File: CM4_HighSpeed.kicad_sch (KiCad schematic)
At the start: 13 parts, among them J10 690-019-298-412, J15 Conn_01x22_Female, J16 Conn_01x22_Female, J22 690-019-298-412, J4 Conn_01x22_Female, J5 Conn_01x22_Female, J6 THD-02-R, U12 RT9742SNGV

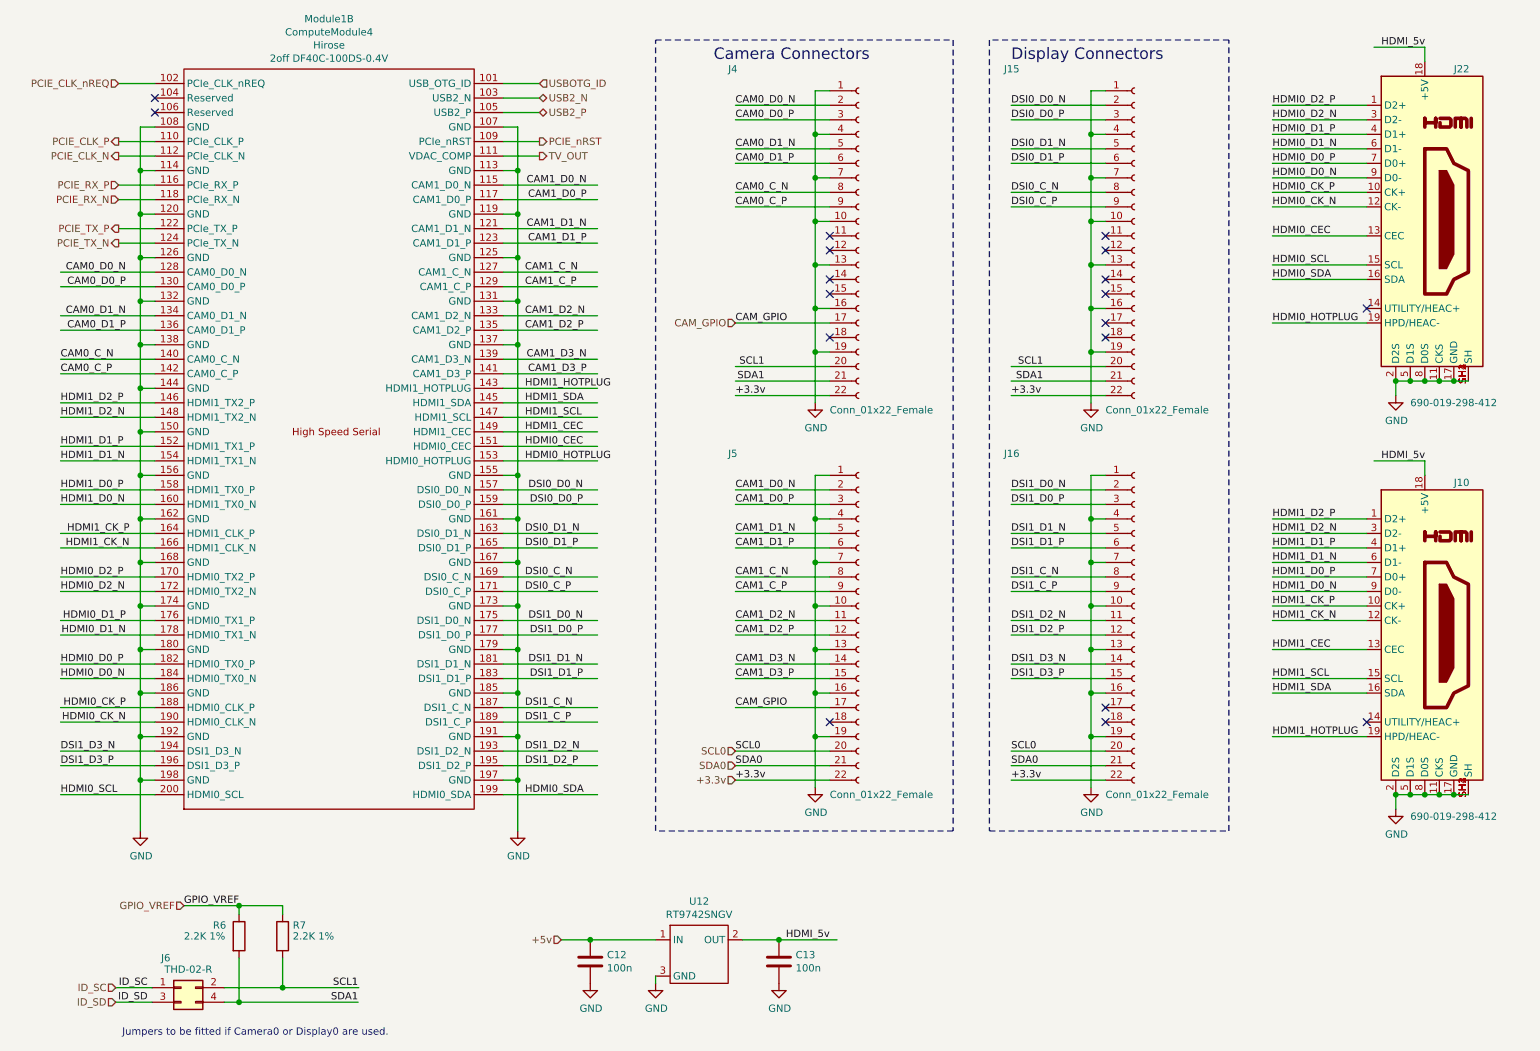
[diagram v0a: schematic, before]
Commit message: removed HDMI, CAM and DISP1 connectors
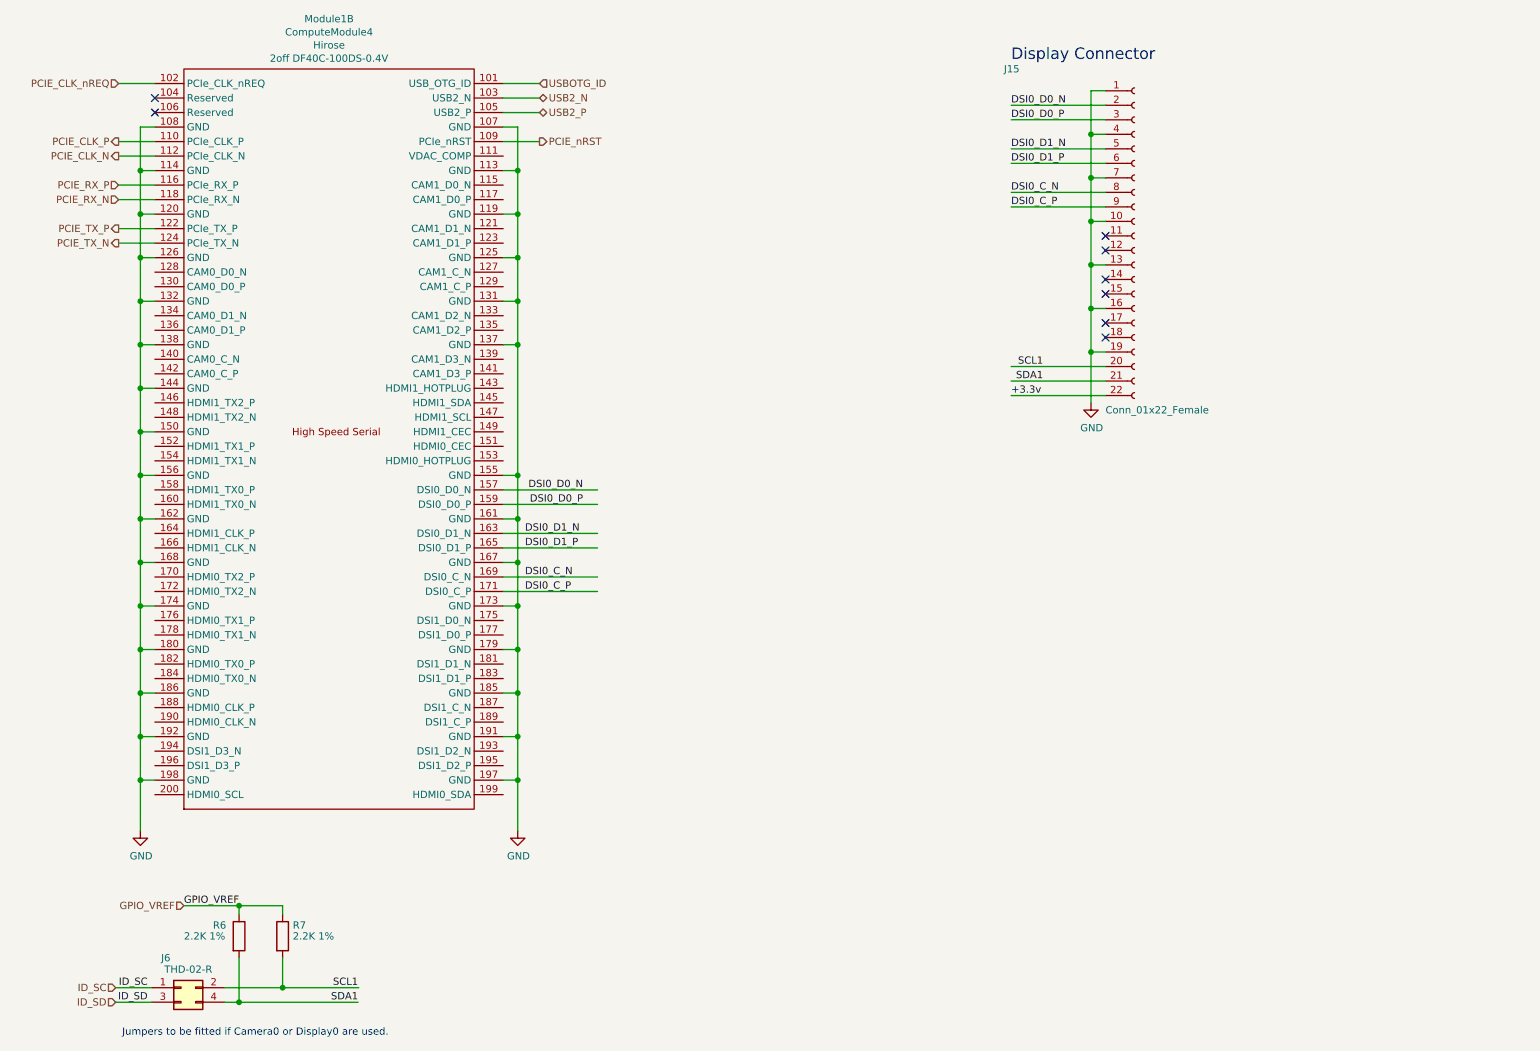
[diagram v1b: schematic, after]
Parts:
- removed C12, C13: 100n, Capacitor_SMD:C_0402_1005Metric, symbol Device:C
- removed J10, J22: 690-019-298-412, CM4IO:EDAC 690-019-298-412, symbol CM4IO:HDMI_A_1.4
- removed J16, J4, J5: Conn_01x22_Female, CM4IO:Hirose_FH12-22S-0.5SH_1x22-1MP_P0.50mm_Horizontal, symbol Connector:Conn_01x22_Female
- removed U12: RT9742SNGV, Package_TO_SOT_SMD:SOT-23, symbol CM4IO:RT9742SNGV
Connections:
- net CAM0_C_N: no longer names the net of Module1.140 (CAM0_C_N)
- net CAM0_C_P: no longer names the net of Module1.142 (CAM0_C_P)
- net CAM0_D0_N: no longer names the net of Module1.128 (CAM0_D0_N)
- net CAM0_D0_P: no longer names the net of Module1.130 (CAM0_D0_P)
- net CAM0_D1_N: no longer names the net of Module1.134 (CAM0_D1_N)
- net CAM0_D1_P: no longer names the net of Module1.136 (CAM0_D1_P)
- net CAM1_C_N: no longer names the net of Module1.127 (CAM1_C_N)
- net CAM1_C_P: no longer names the net of Module1.129 (CAM1_C_P)
- net CAM1_D0_N: no longer names the net of Module1.115 (CAM1_D0_N)
- net CAM1_D0_P: no longer names the net of Module1.117 (CAM1_D0_P)
- net CAM1_D1_N: no longer names the net of Module1.121 (CAM1_D1_N)
- net CAM1_D1_P: no longer names the net of Module1.123 (CAM1_D1_P)
- net CAM1_D2_N: no longer names the net of Module1.133 (CAM1_D2_N)
- net CAM1_D2_P: no longer names the net of Module1.135 (CAM1_D2_P)
- net CAM1_D3_N: no longer names the net of Module1.139 (CAM1_D3_N)
- net CAM1_D3_P: no longer names the net of Module1.141 (CAM1_D3_P)
- net DSI1_C_N: no longer names the net of Module1.187 (DSI1_C_N)
- net DSI1_C_P: no longer names the net of Module1.189 (DSI1_C_P)
- net DSI1_D0_N: no longer names the net of Module1.175 (DSI1_D0_N)
- net DSI1_D0_P: no longer names the net of Module1.177 (DSI1_D0_P)
- net DSI1_D1_N: no longer names the net of Module1.181 (DSI1_D1_N)
- net DSI1_D1_P: no longer names the net of Module1.183 (DSI1_D1_P)
- net DSI1_D2_N: no longer names the net of Module1.193 (DSI1_D2_N)
- net DSI1_D2_P: no longer names the net of Module1.195 (DSI1_D2_P)
- net DSI1_D3_N: no longer names the net of Module1.194 (DSI1_D3_N)
- net DSI1_D3_P: no longer names the net of Module1.196 (DSI1_D3_P)
- net HDMI0_CEC: no longer names the net of Module1.151 (HDMI0_CEC)
- net HDMI0_CK_N: no longer names the net of Module1.190 (HDMI0_CLK_N)
- net HDMI0_CK_P: no longer names the net of Module1.188 (HDMI0_CLK_P)
- net HDMI0_D0_N: no longer names the net of Module1.184 (HDMI0_TX0_N)
- net HDMI0_D0_P: no longer names the net of Module1.182 (HDMI0_TX0_P)
- net HDMI0_D1_N: no longer names the net of Module1.178 (HDMI0_TX1_N)
- net HDMI0_D1_P: no longer names the net of Module1.176 (HDMI0_TX1_P)
- net HDMI0_D2_N: no longer names the net of Module1.172 (HDMI0_TX2_N)
- net HDMI0_D2_P: no longer names the net of Module1.170 (HDMI0_TX2_P)
- net HDMI0_HOTPLUG: no longer names the net of Module1.153 (HDMI0_HOTPLUG)
- net HDMI0_SCL: no longer names the net of Module1.200 (HDMI0_SCL)
- net HDMI0_SDA: no longer names the net of Module1.199 (HDMI0_SDA)
- net HDMI1_CEC: no longer names the net of Module1.149 (HDMI1_CEC)
- net HDMI1_CK_N: no longer names the net of Module1.166 (HDMI1_CLK_N)
- net HDMI1_CK_P: no longer names the net of Module1.164 (HDMI1_CLK_P)
- net HDMI1_D0_N: no longer names the net of Module1.160 (HDMI1_TX0_N)
- net HDMI1_D0_P: no longer names the net of Module1.158 (HDMI1_TX0_P)
- net HDMI1_D1_N: no longer names the net of Module1.154 (HDMI1_TX1_N)
- net HDMI1_D1_P: no longer names the net of Module1.152 (HDMI1_TX1_P)
- net HDMI1_D2_N: no longer names the net of Module1.148 (HDMI1_TX2_N)
- net HDMI1_D2_P: no longer names the net of Module1.146 (HDMI1_TX2_P)
- net HDMI1_HOTPLUG: no longer names the net of Module1.143 (HDMI1_HOTPLUG)
- net HDMI1_SCL: no longer names the net of Module1.147 (HDMI1_SCL)
- net HDMI1_SDA: no longer names the net of Module1.145 (HDMI1_SDA)
- net TV_OUT: no longer names the net of Module1.111 (VDAC_COMP)
- no-connect marks 18 -> 8
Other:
- note added: "Display Connector"
- note removed: "Camera Connectors"
- note removed: "Display Connectors"
- company: © 2020-2022 Raspberry Pi Ltd (formerly Raspberry Pi (Trading) Ltd.) -> (none)
- title: Compute Module 4 IO Board - CM4 - Highspeed -> Bitcart

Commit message: extended the board to make room for IO connectors. added the vertical display connector.
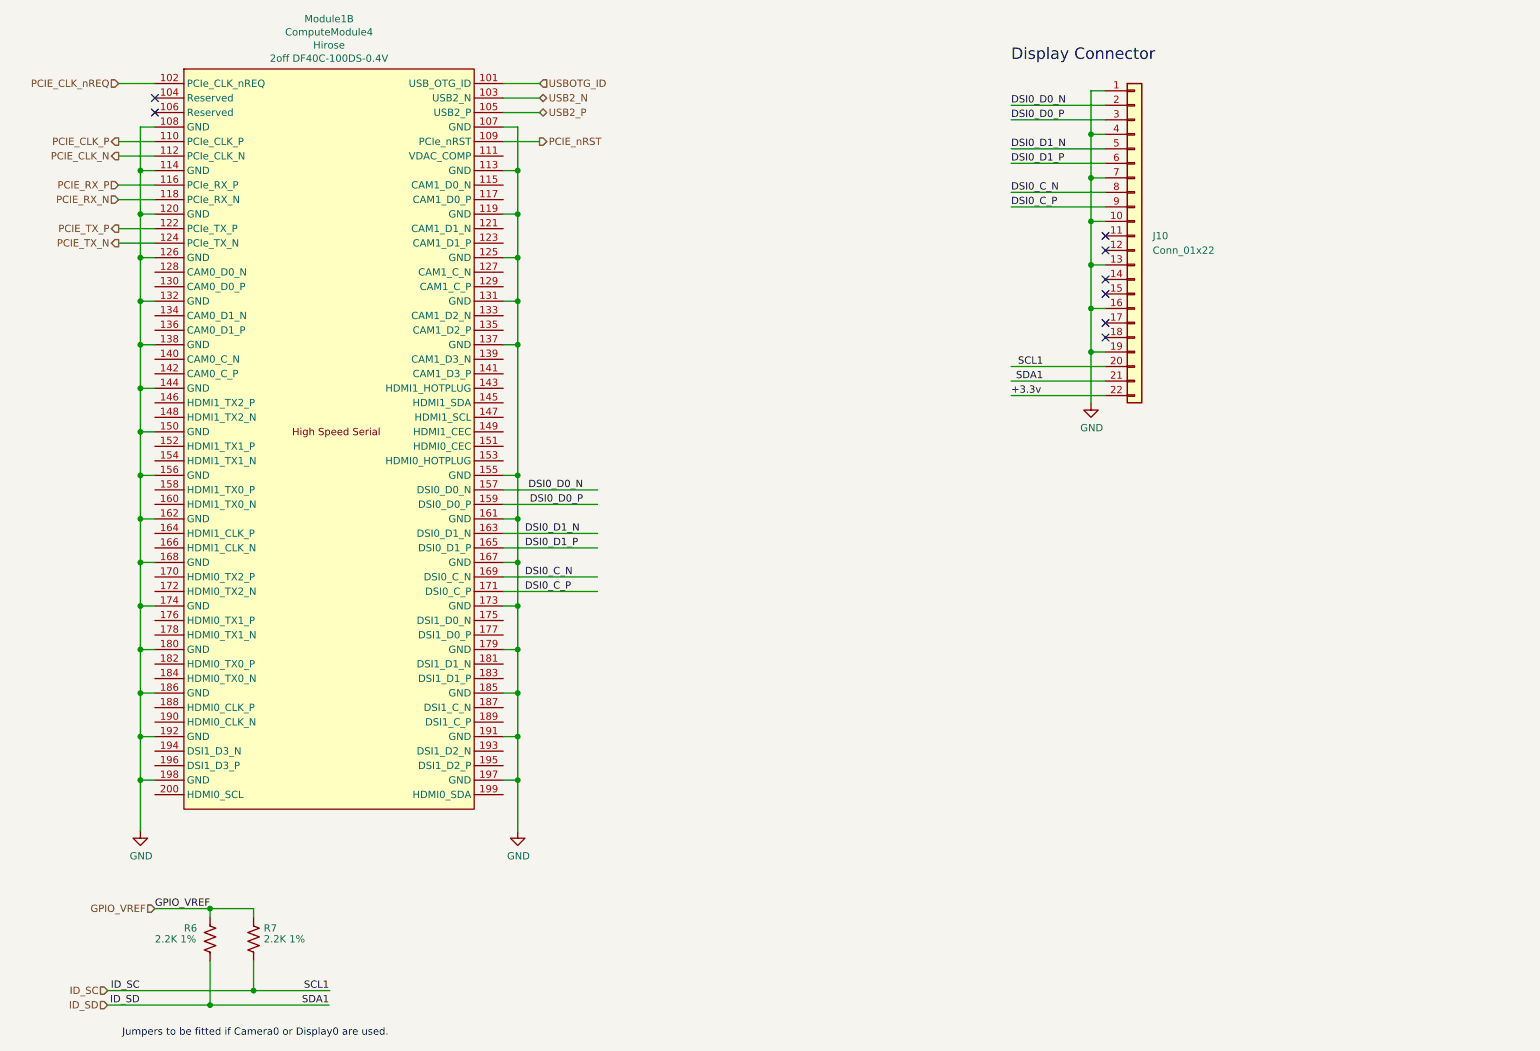
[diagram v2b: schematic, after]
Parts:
- removed J15: Conn_01x22_Female, CM4IO:Hirose_FH12-22S-0.5SH_1x22-1MP_P0.50mm_Horizontal, symbol Connector:Conn_01x22_Female
- removed J6: THD-02-R, Connector_PinHeader_2.54mm:PinHeader_2x02_P2.54mm_Vertical, symbol Connector_Generic:Conn_02x02_Odd_Even
- added J10: Conn_01x22, bitcart:CON22_1X22_DUTB_HRS_HIR, symbol Connector_Generic:Conn_01x22
- R6, R7: symbol Device:R -> Device:R_US
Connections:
- net SCL1 is gone; now on net ID_SC: R7.2
- net SDA1 is gone; now on net ID_SD: R6.2
- net +3.3v: now also J10.22 (Pin_22)
- net DSI0_C_N: now also J10.8 (Pin_8)
- net DSI0_C_P: now also J10.9 (Pin_9)
- net DSI0_D0_N: now also J10.2 (Pin_2)
- net DSI0_D0_P: now also J10.3 (Pin_3)
- net DSI0_D1_N: now also J10.5 (Pin_5)
- net DSI0_D1_P: now also J10.6 (Pin_6)
- net GND: now also J10.1 (Pin_1), J10.10 (Pin_10), J10.13 (Pin_13), J10.16 (Pin_16), J10.19 (Pin_19), J10.4 (Pin_4), J10.7 (Pin_7)
- net ID_SC: now also J10.20 (Pin_20)
- net ID_SD: now also J10.21 (Pin_21)

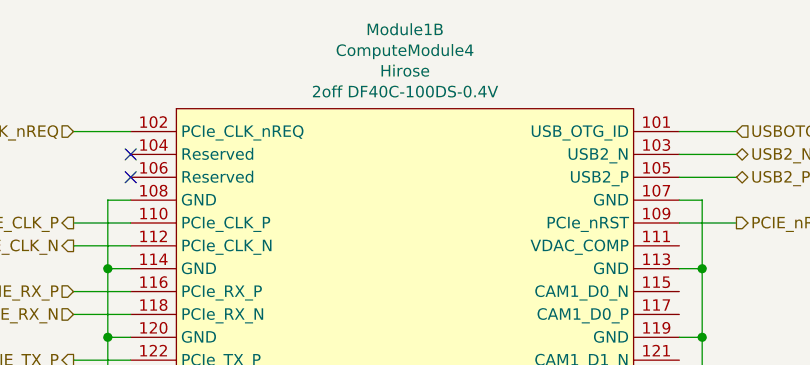
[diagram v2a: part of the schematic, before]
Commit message: finding/adding digikey part numbers
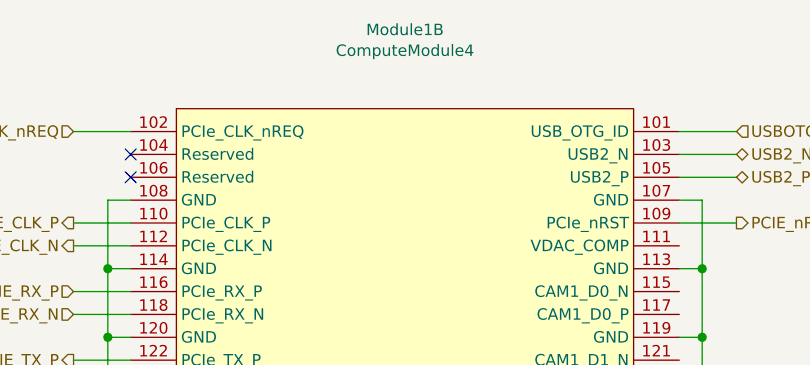
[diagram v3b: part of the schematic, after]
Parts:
- Module1: DK (none) -> 26-DF40C-100DS-0.4V(58)CT-ND; Field4 Hirose -> (none); Field5 2off DF40C-100DS-0.4V -> (none); Field6 2off DF40C-100DS-0.4V -> (none); Field7 Hirose -> (none); PARTNO (none) -> DF40C-100DS-0.4V(58); Part Description 100 Position Connector Receptacle, Center Strip Contacts Su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 -> (none)
- R6, R7: DK (none) -> 311-2.20KLRCT-ND; Field4 Farnell -> (none); Field5 9239278 -> (none); Field6 RK73G1ETQTP2201D -> (none); Field7 KOA EUROPE GMBH -> (none); Field8 120889581 -> (none); PARTNO (none) -> RC0402FR-072K2L; Part Description Resistor 2.2K M1005 1% 63mW -> (none)
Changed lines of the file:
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@@
       (effects (font (size 1.27 1.27)) hide)
     )
-    (property "Field4" "Farnell" (at 51.562 176.403 0)
+    (property "DK" "311-2.20KLRCT-ND" (at 51.562 176.403 0)
       (effects (font (size 1.27 1.27)) hide)
     )
-    (property "Field5" "9239278" (at 51.562 176.403 0)
-      (effects (font (size 1.27 1.27)) hide)
-    )
-    (property "Field7" "KOA EUROPE GMBH" (at 51.562 176.403 0)
-      (effects (font (size 1.27 1.27)) hide)
-    )
-    (property "Field6" "RK73G1ETQTP2201D         " (at 51.562 176.403 0)
-      (effects (font (size 1.27 1.27)) hide)
-    )
-    (property "Part Description" "Resistor 2.2K M1005 1% 63mW" (at 51.562 176.403 0)
-      (effects (font (size 1.27 1.27)) hide)
-    )
-    (property "Field8" "120889581" (at 51.562 176.403 0)
+    (property "PARTNO" "RC0402FR-072K2L" (at 51.562 176.403 0)
       (effects (font (size 1.27 1.27)) hide)
     )
@@
       (effects (font (size 1.27 1.27)) hide)
     )
-    (property "Field4" "Farnell" (at 59.182 176.403 0)
+    (property "PARTNO" "RC0402FR-072K2L" (at 59.182 176.403 0)
       (effects (font (size 1.27 1.27)) hide)
     )
-    (property "Field5" "9239278" (at 59.182 176.403 0)
-      (effects (font (size 1.27 1.27)) hide)
-    )
-    (property "Field7" "KOA EUROPE GMBH" (at 59.182 176.403 0)
-      (effects (font (size 1.27 1.27)) hide)
-    )
-    (property "Field6" "RK73G1ETQTP2201D         " (at 59.182 176.403 0)
-      (effects (font (size 1.27 1.27)) hide)
-    )
-    (property "Part Description" "Resistor 2.2K M1005 1% 63mW" (at 59.182 176.403 0)
-      (effects (font (size 1.27 1.27)) hide)
-    )
-    (property "Field8" "120889581" (at 59.182 176.403 0)
+    (property "DK" "311-2.20KLRCT-ND" (at 59.182 176.403 0)
       (effects (font (size 1.27 1.27)) hide)
     )
@@
       (effects (font (size 1.27 1.27)) hide)
     )
-    (property "Field4" "Hirose" (at 72.39 19.9644 0)
-      (effects (font (size 1.27 1.27)))
-    )
-    (property "Field5" "2off DF40C-100DS-0.4V" (at 72.39 22.2758 0)
-      (effects (font (size 1.27 1.27)))
-    )
-    (property "Field6" "2off DF40C-100DS-0.4V" (at -67.31 87.63 0)
+    (property "DK" "26-DF40C-100DS-0.4V(58)CT-ND" (at -67.31 87.63 0)
       (effects (font (size 1.27 1.27)) hide)
     )
-    (property "Field7" "Hirose" (at -67.31 87.63 0)
+    (property "PARTNO" "DF40C-100DS-0.4V(58)" (at -67.31 87.63 0)
       (effects (font (size 1.27 1.27)) hide)
     )
-    (property "Part Description" "	100 Position Connector Receptacle, Center Strip Contacts Surface Mount Gold" (at -67.31 87.63 0)
-      (effects (font (size 1.27 1.27)) hide)
-    )
